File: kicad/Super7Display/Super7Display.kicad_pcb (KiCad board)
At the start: 2 copper layers, 216.5 x 33 mm, 10 parts, among them P1 CONN_01X13, P2 CONN_01X09

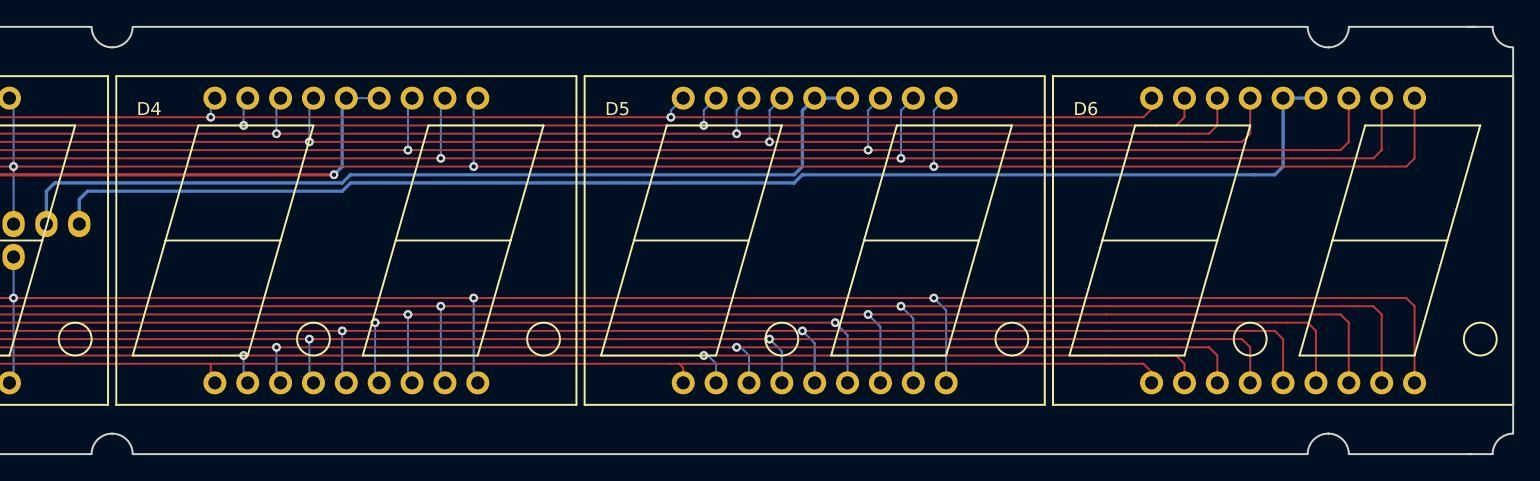
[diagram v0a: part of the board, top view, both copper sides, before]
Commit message: Remove D6 from layout
Move right edge into place
Top and bottom edges still need adjusted
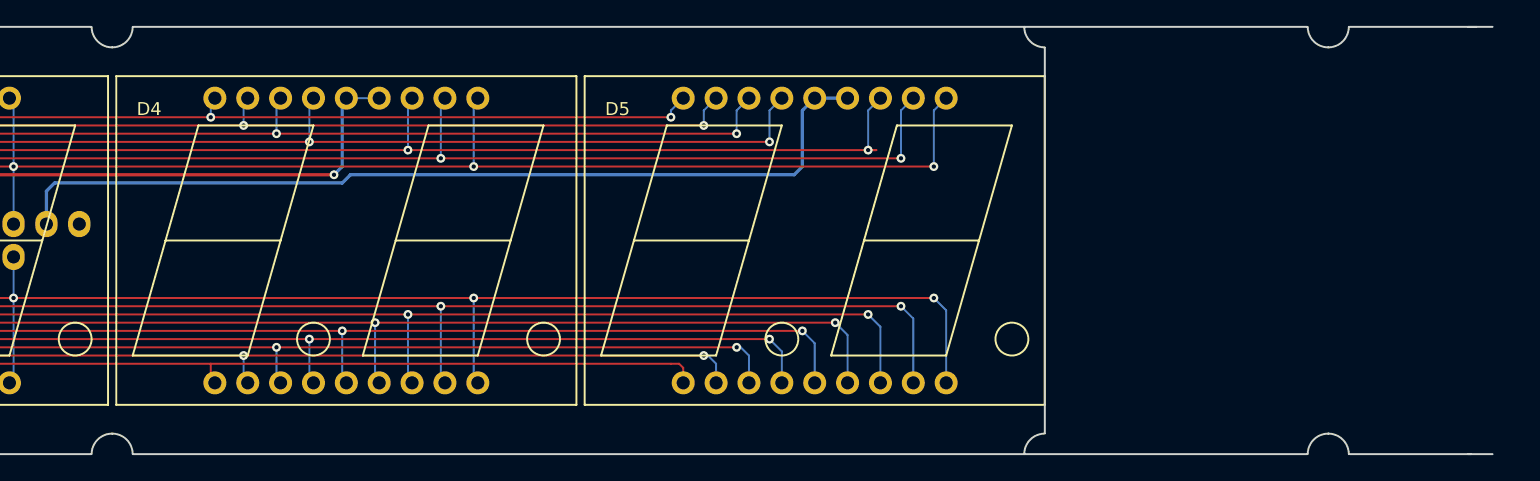
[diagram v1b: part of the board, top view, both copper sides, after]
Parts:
- removed D6: DC08, footprints:DC08
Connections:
- P1 pad 13: DIG6 -> Net-(P1-Pad13)
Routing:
- net DIG6: track 103.8 -> 0.00 mm
- net DP2: track 223.0 -> 179.6 mm
- net C2: track 219.8 -> 177.1 mm
- net G2: track 216.6 -> 174.6 mm
- net B2: track 230.4 -> 188.3 mm
- net A2: track 228.5 -> 187.1 mm
- net D2: track 213.4 -> 172.0 mm
- net F2: track 212.1 -> 171.3 mm
- net E2: track 210.3 -> 169.5 mm
- net DP1: track 207.3 -> 167.1 mm
- net B1: track 207.1 -> 166.9 mm
- net C1: track 204.3 -> 164.8 mm
- net A1: track 203.9 -> 164.4 mm
- net D1: track 201.5 -> 162.6 mm
- net G1: track 200.4 -> 161.6 mm
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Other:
- board size 216.5 x 33 mm -> 214.9 x 33 mm

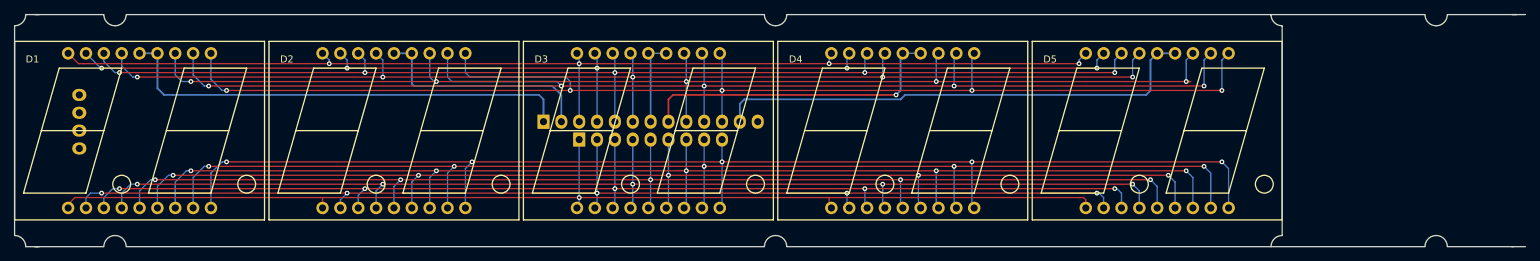
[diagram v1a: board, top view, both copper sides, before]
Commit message: Move mounting tabs above/below D1, D3, D5
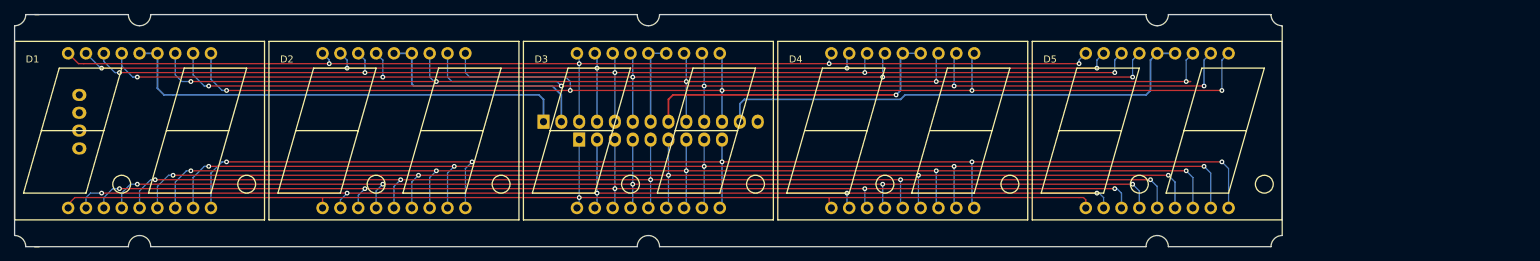
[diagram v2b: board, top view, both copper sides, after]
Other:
- board size 214.9 x 33 mm -> 180.3 x 33 mm
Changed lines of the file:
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@@
     (links 90)
     (no_connects 0)
-    (area 163.548287 44.036001 392.822501 83.895001)
+    (area 163.548287 45.814 356.779901 83.895001)
     (thickness 1.6)
-    (drawings 43)
+    (drawings 40)
     (tracks 343)
     (zones 0)
@@
     )
   )
+  (gr_line (start 195.58 83.82) (end 264.795 83.82) (angle 90) (layer Edge.Cuts) (width 0.15))
+  (gr_line (start 337.185 83.82) (end 267.97 83.82) (angle 90) (layer Edge.Cuts) (width 0.15))
+  (gr_line (start 354.965 83.82) (end 340.36 83.82) (angle 90) (layer Edge.Cuts) (width 0.15))
+  (gr_line (start 340.36 50.8) (end 354.965 50.8) (angle 90) (layer Edge.Cuts) (width 0.15))
+  (gr_line (start 267.97 50.8) (end 337.185 50.8) (angle 90) (layer Edge.Cuts) (width 0.15))
+  (gr_line (start 195.58 50.8) (end 264.795 50.8) (angle 90) (layer Edge.Cuts) (width 0.15))
   (dimension 180.34 (width 0.3) (layer F.Fab)
     (gr_text "7.1000 in" (at 266.319 47.164) (layer F.Fab)
@@
   (gr_line (start 179.07 50.8) (end 179.705 50.8) (angle 90) (layer Edge.Cuts) (width 0.15))
   (gr_line (start 179.07 83.82) (end 179.705 83.82) (angle 90) (layer Edge.Cuts) (width 0.15))
-  (gr_line (start 391.16 83.82) (end 389.255 83.82) (angle 90) (layer Edge.Cuts) (width 0.15))
-  (gr_line (start 389.255 50.8) (end 389.89 50.8) (angle 90) (layer Edge.Cuts) (width 0.15))
-  (gr_line (start 391.16 50.8) (end 389.5725 50.8) (angle 90) (layer Edge.Cuts) (width 0.15))
   (gr_line (start 177.8 83.82) (end 179.3875 83.82) (angle 90) (layer Edge.Cuts) (width 0.15))
   (gr_line (start 177.8 50.8) (end 179.3875 50.8) (angle 90) (layer Edge.Cuts) (width 0.15))
-  (gr_line (start 389.509 50.8) (end 380.111 50.8) (angle 90) (layer Edge.Cuts) (width 0.15))
   (gr_line (start 356.5525 82.169) (end 356.5525 52.451) (angle 90) (layer Edge.Cuts) (width 0.15))
-  (gr_line (start 380.111 83.82) (end 389.509 83.82) (angle 90) (layer Edge.Cuts) (width 0.15))
   (gr_arc (start 356.5525 83.82) (end 354.965 83.82) (angle 90) (layer Edge.Cuts) (width 0.15))
   (gr_arc (start 356.5525 50.8) (end 356.5525 52.3875) (angle 90) (layer Edge.Cuts) (width 0.15))
-  (gr_line (start 179.451 83.82) (end 188.849 83.82) (angle 90) (layer Edge.Cuts) (width 0.15))
-  (gr_line (start 179.451 50.8) (end 188.849 50.8) (angle 90) (layer Edge.Cuts) (width 0.15))
+  (gr_line (start 179.451 83.82) (end 192.405 83.82) (angle 90) (layer Edge.Cuts) (width 0.15))
+  (gr_line (start 179.451 50.8) (end 192.405 50.8) (angle 90) (layer Edge.Cuts) (width 0.15))
   (gr_line (start 176.2125 52.451) (end 176.2125 57.15) (angle 90) (layer Edge.Cuts) (width 0.15))
   (gr_line (start 176.2125 82.169) (end 176.2125 78.105) (angle 90) (layer Edge.Cuts) (width 0.15))
   (gr_arc (start 176.2125 83.82) (end 176.2125 82.2325) (angle 90) (layer Edge.Cuts) (width 0.15))
   (gr_arc (start 176.2125 50.8) (end 177.8 50.8) (angle 90) (layer Edge.Cuts) (width 0.15))
-  (gr_line (start 286.131 50.8) (end 376.809 50.8) (angle 90) (layer Edge.Cuts) (width 0.15))
-  (gr_line (start 192.151 50.8) (end 282.829 50.8) (angle 90) (layer Edge.Cuts) (width 0.15))
-  (gr_line (start 282.829 83.82) (end 192.151 83.82) (angle 90) (layer Edge.Cuts) (width 0.15))
-  (gr_line (start 286.131 83.82) (end 376.809 83.82) (angle 90) (layer Edge.Cuts) (width 0.15))
-  (gr_arc (start 284.48 50.8) (end 284.48 52.3875) (angle 90) (layer Edge.Cuts) (width 0.15))
-  (gr_arc (start 378.46 50.8) (end 378.46 52.3875) (angle 90) (layer Edge.Cuts) (width 0.15))
-  (gr_arc (start 378.46 50.8) (end 380.0475 50.8) (angle 90) (layer Edge.Cuts) (width 0.15))
-  (gr_arc (start 378.46 83.82) (end 376.8725 83.82) (angle 90) (layer Edge.Cuts) (width 0.15))
-  (gr_arc (start 378.46 83.82) (end 378.46 82.2325) (angle 90) (layer Edge.Cuts) (width 0.15))
-  (gr_arc (start 190.5 83.82) (end 190.5 82.2325) (angle 90) (layer Edge.Cuts) (width 0.15))
-  (gr_arc (start 190.5 83.82) (end 188.9125 83.82) (angle 90) (layer Edge.Cuts) (width 0.15))
-  (gr_arc (start 190.5 50.8) (end 192.0875 50.8) (angle 90) (layer Edge.Cuts) (width 0.15))
-  (gr_arc (start 190.5 50.8) (end 190.5 52.3875) (angle 90) (layer Edge.Cuts) (width 0.15))
+  (gr_arc (start 266.3825 50.8) (end 266.3825 52.3875) (angle 90) (layer Edge.Cuts) (width 0.15))
+  (gr_arc (start 338.7725 50.8) (end 338.7725 52.3875) (angle 90) (layer Edge.Cuts) (width 0.15))
+  (gr_arc (start 338.7725 50.8) (end 340.36 50.8) (angle 90) (layer Edge.Cuts) (width 0.15))
+  (gr_arc (start 338.7725 83.82) (end 337.185 83.82) (angle 90) (layer Edge.Cuts) (width 0.15))
+  (gr_arc (start 338.7725 83.82) (end 338.7725 82.2325) (angle 90) (layer Edge.Cuts) (width 0.15))
+  (gr_arc (start 193.9925 83.82) (end 193.9925 82.2325) (angle 90) (layer Edge.Cuts) (width 0.15))
+  (gr_arc (start 193.9925 83.82) (end 192.405 83.82) (angle 90) (layer Edge.Cuts) (width 0.15))
+  (gr_arc (start 193.9925 50.8) (end 195.58 50.8) (angle 90) (layer Edge.Cuts) (width 0.15))
+  (gr_arc (start 193.9925 50.8) (end 193.9925 52.3875) (angle 90) (layer Edge.Cuts) (width 0.15))
   (gr_line (start 176.2125 62.23) (end 176.2125 57.15) (angle 90) (layer Edge.Cuts) (width 0.15))
   (gr_line (start 176.2125 72.39) (end 176.2125 78.105) (angle 90) (layer Edge.Cuts) (width 0.15))
@@
     (effects (font (size 1.5 1.5) (thickness 0.3)) (justify mirror))
   )
-  (gr_arc (start 284.48 83.82) (end 282.8925 83.82) (angle 90) (layer Edge.Cuts) (width 0.15))
-  (gr_arc (start 284.48 83.82) (end 284.48 82.2325) (angle 90) (layer Edge.Cuts) (width 0.15))
-  (gr_arc (start 284.48 50.8) (end 286.0675 50.8) (angle 90) (layer Edge.Cuts) (width 0.15))
+  (gr_arc (start 266.3825 83.82) (end 264.795 83.82) (angle 90) (layer Edge.Cuts) (width 0.15))
+  (gr_arc (start 266.3825 83.82) (end 266.3825 82.2325) (angle 90) (layer Edge.Cuts) (width 0.15))
+  (gr_arc (start 266.3825 50.8) (end 267.97 50.8) (angle 90) (layer Edge.Cuts) (width 0.15))
   (gr_line (start 176.2125 62.23) (end 176.2125 72.39) (angle 90) (layer Edge.Cuts) (width 0.15))
   (segment (start 186.055 76.835) (end 184.785 76.835) (width 0.1524) (layer F.Cu) (net 1))

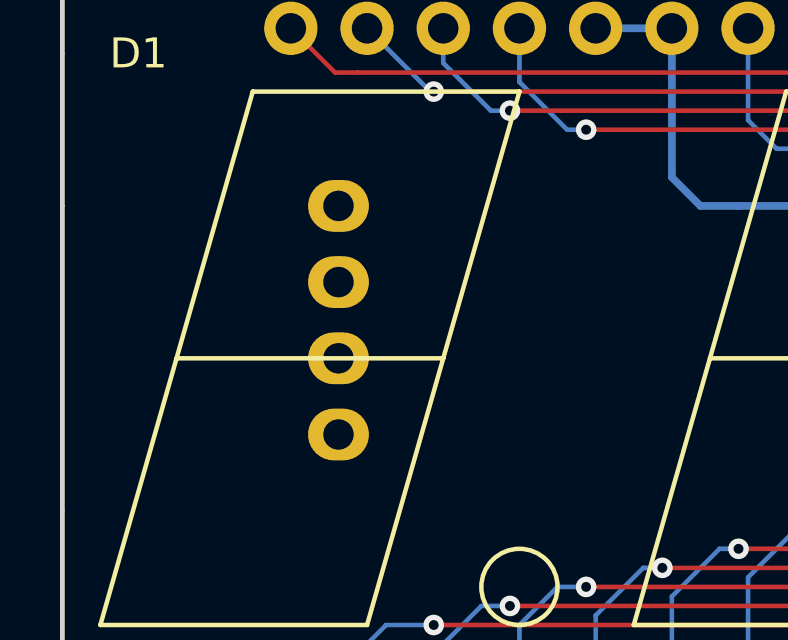
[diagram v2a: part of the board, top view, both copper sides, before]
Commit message: add anchor to display also
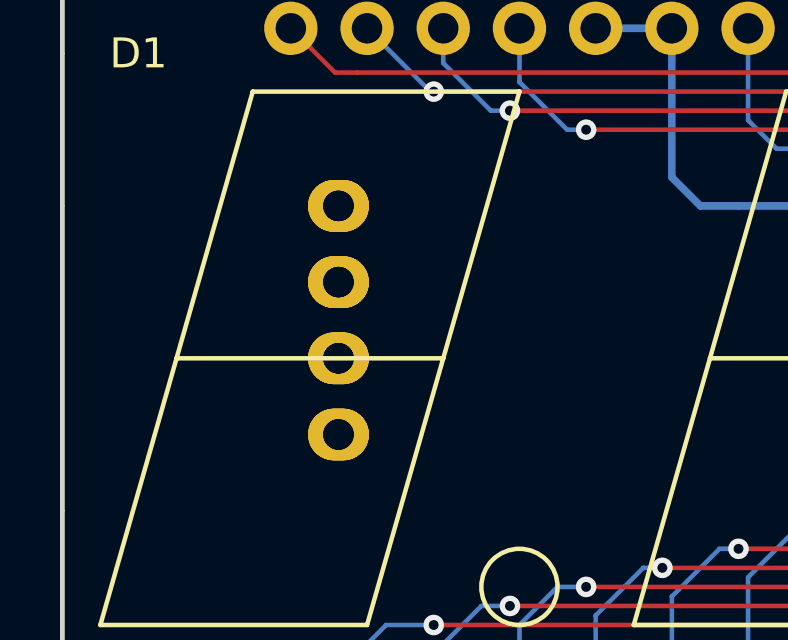
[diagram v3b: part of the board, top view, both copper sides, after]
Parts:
- removed the REF** at (185.4, 69.8)
- added REF** (x2): Socket_Strip_Straight_1x04, misc:Strip_1x04, F.Cu at (185.4, 69.8)
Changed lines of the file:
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@@
+    )
+  )
+  (module misc:Strip_1x04 (layer F.Cu)
+    (at 185.42 69.85 90)
+    (descr "Through hole socket strip")
+    (tags "socket strip")
+    (fp_text reference REF** (at 0 -5.1 90) (layer F.SilkS) hide
+      (effects (font (size 1 1) (thickness 0.15)))
+    )
+    (fp_text value Socket_Strip_Straight_1x04 (at 0 -3.1 90) (layer F.Fab) hide
+      (effects (font (size 1 1) (thickness 0.15)))
+    )
+    (fp_line (start -1.75 -1.75) (end -1.75 1.75) (layer F.CrtYd) (width 0.05))
+    (fp_line (start 9.4 -1.75) (end 9.4 1.75) (layer F.CrtYd) (width 0.05))
+    (fp_line (start -1.75 -1.75) (end 9.4 -1.75) (layer F.CrtYd) (width 0.05))
+    (fp_line (start -1.75 1.75) (end 9.4 1.75) (layer F.CrtYd) (width 0.05))
+    (pad 1 thru_hole oval (at 0 0 90) (size 1.7272 2.032) (drill 1.016) (layers *.Cu *.Mask))
+    (pad 2 thru_hole oval (at 2.54 0 90) (size 1.7272 2.032) (drill 1.016) (layers *.Cu *.Mask))
+    (pad 3 thru_hole oval (at 5.08 0 90) (size 1.7272 2.032) (drill 1.016) (layers *.Cu *.Mask))
+    (pad 4 thru_hole oval (at 7.62 0 90) (size 1.7272 2.032) (drill 1.016) (layers *.Cu *.Mask))
+    (model Socket_Strips.3dshapes/Socket_Strip_Straight_1x04.wrl
+      (at (xyz 0.15 0 0))
+      (scale (xyz 1 1 1))
+      (rotate (xyz 0 0 180))
     )
   )

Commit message: remove anchor and change silkscreen
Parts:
- removed REF** (x2): Socket_Strip_Straight_1x04, misc:Strip_1x04
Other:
- board text added: "Maniacal Labs Super 7 Segment 10 Digit Display remixed by @Dillon1337 tinkerer.us"
- board text removed: "Anchor This Side"
- board text removed: "Maniacal Labs Super 7 Segment Display"
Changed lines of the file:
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@@
     (area 163.548287 45.814 356.779901 83.895001)
     (thickness 1.6)
-    (drawings 40)
+    (drawings 39)
     (tracks 343)
     (zones 0)
-    (modules 9)
+    (modules 8)
     (nets 23)
   )
@@
     (34 B.Paste user)
     (35 F.Paste user)
-    (36 B.SilkS user hide)
+    (36 B.SilkS user)
     (37 F.SilkS user)
     (38 B.Mask user)
@@
       (xy 0.280132 4.064859)) (layer B.SilkS) (width 0.01))
   )
-  (module misc:Strip_1x04 (layer F.Cu)
-    (at 185.42 69.85 90)
-    (descr "Through hole socket strip")
-    (tags "socket strip")
-    (fp_text reference REF** (at 0 -5.1 90) (layer F.SilkS) hide
-      (effects (font (size 1 1) (thickness 0.15)))
-    )
-    (fp_text value Socket_Strip_Straight_1x04 (at 0 -3.1 90) (layer F.Fab) hide
-      (effects (font (size 1 1) (thickness 0.15)))
-    )
-    (fp_line (start -1.75 -1.75) (end -1.75 1.75) (layer F.CrtYd) (width 0.05))
-    (fp_line (start 9.4 -1.75) (end 9.4 1.75) (layer F.CrtYd) (width 0.05))
-    (fp_line (start -1.75 -1.75) (end 9.4 -1.75) (layer F.CrtYd) (width 0.05))
-    (fp_line (start -1.75 1.75) (end 9.4 1.75) (layer F.CrtYd) (width 0.05))
-    (pad 1 thru_hole oval (at 0 0 90) (size 1.7272 2.032) (drill 1.016) (layers *.Cu *.Mask))
-    (pad 2 thru_hole oval (at 2.54 0 90) (size 1.7272 2.032) (drill 1.016) (layers *.Cu *.Mask))
-    (pad 3 thru_hole oval (at 5.08 0 90) (size 1.7272 2.032) (drill 1.016) (layers *.Cu *.Mask))
-    (pad 4 thru_hole oval (at 7.62 0 90) (size 1.7272 2.032) (drill 1.016) (layers *.Cu *.Mask))
-    (model Socket_Strips.3dshapes/Socket_Strip_Straight_1x04.wrl
-      (at (xyz 0.15 0 0))
-      (scale (xyz 1 1 1))
-      (rotate (xyz 0 0 180))
-    )
-  )
   (module footprints:DC08 (layer F.Cu)
     (at 193.9925 67.31)
@@
     )
   )
-  (module misc:Strip_1x04 (layer F.Cu)
-    (at 185.42 69.85 90)
-    (descr "Through hole socket strip")
-    (tags "socket strip")
-    (fp_text reference REF** (at 0 -5.1 90) (layer F.SilkS) hide
-      (effects (font (size 1 1) (thickness 0.15)))
-    )
-    (fp_text value Socket_Strip_Straight_1x04 (at 0 -3.1 90) (layer F.Fab) hide
-      (effects (font (size 1 1) (thickness 0.15)))
-    )
-    (fp_line (start -1.75 -1.75) (end -1.75 1.75) (layer F.CrtYd) (width 0.05))
-    (fp_line (start 9.4 -1.75) (end 9.4 1.75) (layer F.CrtYd) (width 0.05))
-    (fp_line (start -1.75 -1.75) (end 9.4 -1.75) (layer F.CrtYd) (width 0.05))
-    (fp_line (start -1.75 1.75) (end 9.4 1.75) (layer F.CrtYd) (width 0.05))
-    (pad 1 thru_hole oval (at 0 0 90) (size 1.7272 2.032) (drill 1.016) (layers *.Cu *.Mask))
-    (pad 2 thru_hole oval (at 2.54 0 90) (size 1.7272 2.032) (drill 1.016) (layers *.Cu *.Mask))
-    (pad 3 thru_hole oval (at 5.08 0 90) (size 1.7272 2.032) (drill 1.016) (layers *.Cu *.Mask))
-    (pad 4 thru_hole oval (at 7.62 0 90) (size 1.7272 2.032) (drill 1.016) (layers *.Cu *.Mask))
-    (model Socket_Strips.3dshapes/Socket_Strip_Straight_1x04.wrl
-      (at (xyz 0.15 0 0))
-      (scale (xyz 1 1 1))
-      (rotate (xyz 0 0 180))
-    )
-  )
   (gr_line (start 195.58 83.82) (end 264.795 83.82) (angle 90) (layer Edge.Cuts) (width 0.15))
   (gr_line (start 337.185 83.82) (end 267.97 83.82) (angle 90) (layer Edge.Cuts) (width 0.15))
@@
   (gr_line (start 176.2125 62.23) (end 176.2125 57.15) (angle 90) (layer Edge.Cuts) (width 0.15))
   (gr_line (start 176.2125 72.39) (end 176.2125 78.105) (angle 90) (layer Edge.Cuts) (width 0.15))
-  (gr_text "Anchor This Side" (at 187.96 66.04 90) (layer B.SilkS)
-    (effects (font (size 0.762 0.762) (thickness 0.1905)) (justify mirror))
-  )
   (gr_text "Controller Header This Side" (at 266.7 62.865) (layer B.SilkS)
     (effects (font (size 1.016 1.016) (thickness 0.254)) (justify mirror))
   )
-  (gr_text "Maniacal Labs\nSuper 7 Segment\nDisplay" (at 330.835 67.31) (layer B.SilkS)
-    (effects (font (size 1.5 1.5) (thickness 0.3)) (justify mirror))
+  (gr_text "Maniacal Labs\nSuper 7 Segment\n10 Digit Display\nremixed by\n@Dillon1337\ntinkerer.us" (at 330.835 67.31) (layer B.SilkS)
+    (effects (font (size 1.5 1.5) (thickness 0.2)) (justify mirror))
   )
   (gr_arc (start 266.3825 83.82) (end 264.795 83.82) (angle 90) (layer Edge.Cuts) (width 0.15))

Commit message: change page size and move into center
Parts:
- moved P2 126.8 mm to (130.8, 85.1)
- moved D1 126.8 mm to (68.3, 83.8)
- moved D2 126.8 mm to (104.5, 83.8)
- moved P1 126.8 mm to (125.7, 82.5)
- moved D3 126.8 mm to (140.7, 83.8)
- moved D4 126.8 mm to (176.8, 83.8)
- moved D5 126.8 mm to (213.0, 83.8)
- moved G*** 126.8 mm to (220.3, 83.8)
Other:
- outline, holes or cut-outs redrawn
